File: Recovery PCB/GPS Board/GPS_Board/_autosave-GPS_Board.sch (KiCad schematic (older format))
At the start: 11 parts, among them J1 XT30-M, J2 XT30-M, U1 Teensy4.1

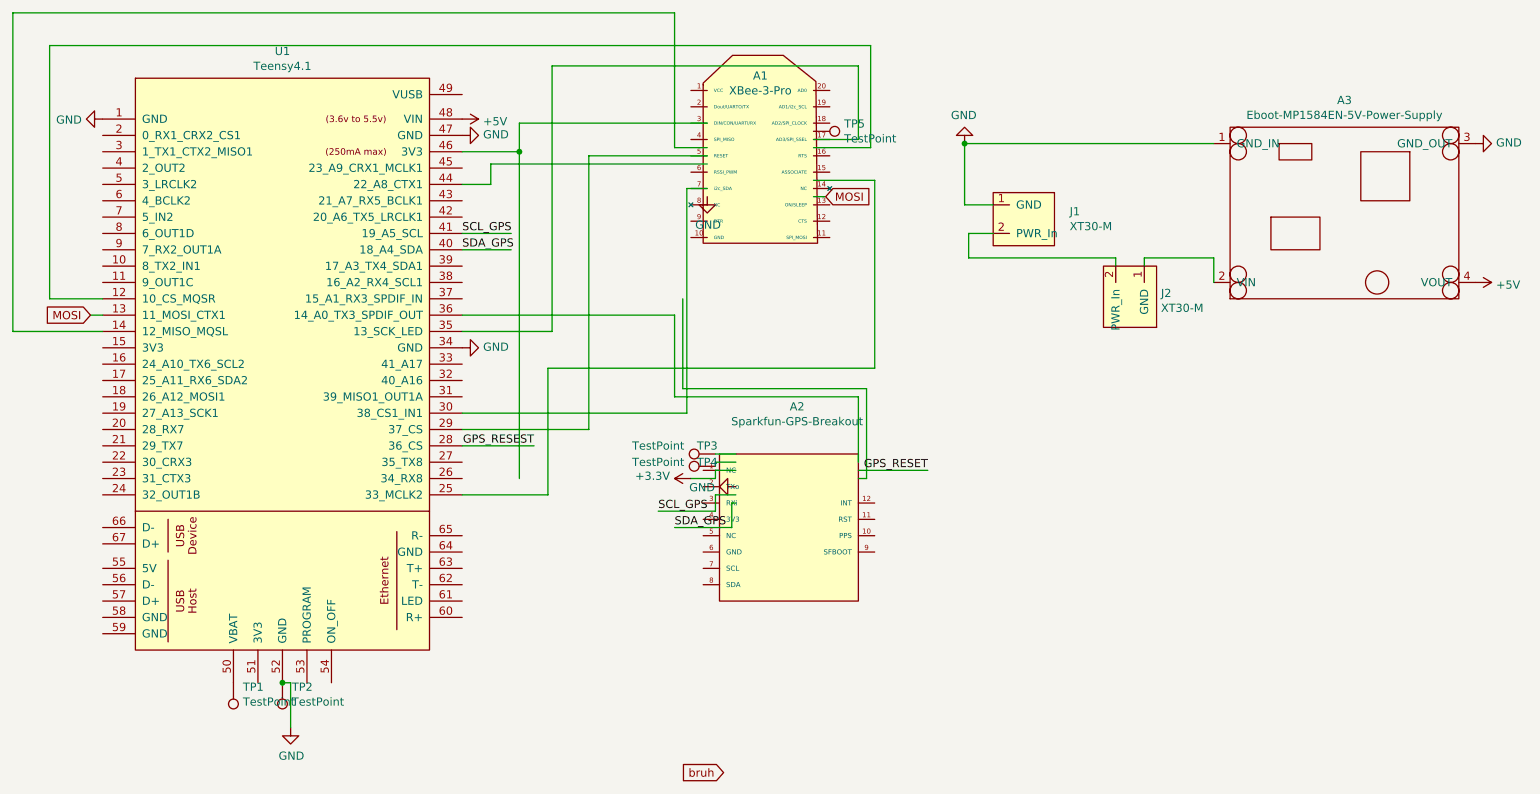
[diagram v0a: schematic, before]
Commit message: replace all wires w labels
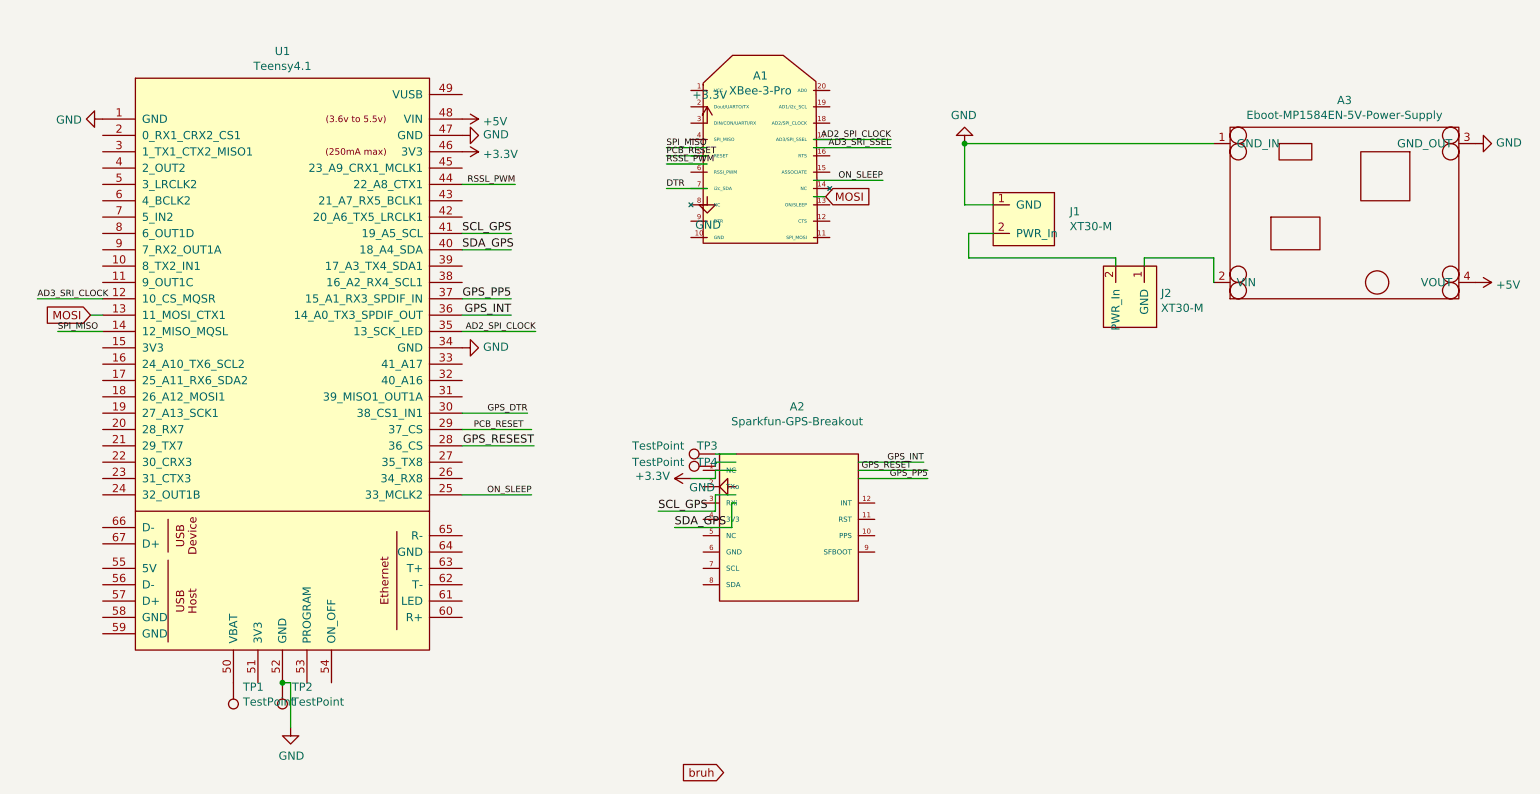
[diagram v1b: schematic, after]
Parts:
- removed TP5: TestPoint, TestPoint:TestPoint_Pad_D1.0mm, symbol Connector:TestPoint
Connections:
- net labels added: AD2_SPI_CLOCK, AD3_SRI_CLOCK, AD3_SRI_SSEL, DTR, GPS_DTR, GPS_INT, GPS_PP5, ON_SLEEP, PCB_RESET, RSSL_PWM, SPI_MISO
- wire segments 71 -> 48
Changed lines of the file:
@@
 	0    1    1    0
 $EndComp
-Wire Wire Line
-	4350 3600 4350 1600
-Wire Wire Line
-	4350 1600 4000 1600
 $Comp
 L power:GND #PWR0102
@@
 $EndComp
 Wire Wire Line
-	5300 3100 5300 2600
-Wire Wire Line
-	5300 2600 4000 2600
-Wire Wire Line
-	5350 2500 5350 3050
-Wire Wire Line
-	5350 3050 6475 3050
-Wire Wire Line
-	6475 3050 6475 3600
-Wire Wire Line
-	6475 3600 6425 3600
-Wire Wire Line
 	2900 4850 2950 4850
 Wire Wire Line
@@
 	1    0    0    -1
 $EndComp
-Wire Wire Line
-	5500 1425 4350 1425
-Wire Wire Line
-	4350 1425 4350 1600
-Connection ~ 4350 1600
-$Comp
-L Connector:TestPoint TP5
-U 1 1 61AB1BEF
-P 6150 1475
-F 0 "TP5" V 6104 1663 50  0000 L CNN
-F 1 "TestPoint" V 6195 1663 50  0000 L CNN
-F 2 "TestPoint:TestPoint_Pad_D1.0mm" H 6350 1475 50  0001 C CNN
-F 3 "~" H 6350 1475 50  0001 C CNN
-	1    6150 1475
-	0    1    1    0
-$EndComp
-Wire Wire Line
-	5500 1575 5300 1575
-Wire Wire Line
-	5300 1575 5300 750
-Wire Wire Line
-	5300 750  1250 750
-Wire Wire Line
-	1250 750  1250 2700
-Wire Wire Line
-	1250 2700 1800 2700
-Wire Wire Line
-	5500 1675 4175 1675
-Wire Wire Line
-	4175 1675 4175 1800
-Wire Wire Line
-	4175 1800 4000 1800
-Wire Wire Line
-	5500 1625 4775 1625
-Wire Wire Line
-	4775 1625 4775 3300
-Wire Wire Line
-	4775 3300 4000 3300
-Wire Wire Line
-	5500 1825 5375 1825
-Wire Wire Line
-	5375 1825 5375 3200
-Wire Wire Line
-	5375 3200 4000 3200
-Wire Wire Line
-	1800 2500 1475 2500
-Wire Wire Line
-	1475 2500 1475 950
-Wire Wire Line
-	1475 950  6500 950
-Wire Wire Line
-	6500 950  6500 1575
-Wire Wire Line
-	6500 1575 6150 1575
-Wire Wire Line
-	6150 1525 6425 1525
-Wire Wire Line
-	6425 1525 6425 1075
-Wire Wire Line
-	6425 1075 4550 1075
-Wire Wire Line
-	4550 1075 4550 2700
-Wire Wire Line
-	4550 2700 4000 2700
-Wire Wire Line
-	4525 2925 4525 3700
-Wire Wire Line
-	4525 3700 4000 3700
 Text GLabel 6225 1875 2    50   Input ~ 0
 MOSI
 Wire Wire Line
 	6150 1875 6225 1875
-Wire Wire Line
-	6150 1775 6525 1775
-Wire Wire Line
-	4525 2925 6525 2925
-Wire Wire Line
-	6525 1775 6525 2925
 Text GLabel 1725 2600 0    50   Input ~ 0
 MOSI
@@
 	0    -1   -1   0
 $EndComp
-Wire Wire Line
-	6425 3500 6425 3100
-Wire Wire Line
-	6425 3100 5300 3100
 Text GLabel 5600 5400 0    50   Input ~ 0
 bruh
@@
 Wire Wire Line
 	4000 3400 4440 3400
-Text Label 6850 3550 2    50   ~ 0
+Text Label 6750 3550 2    39   ~ 0
 GPS_RESET
 Wire Wire Line
 	6425 3550 6850 3550
+Wire Wire Line
+	6425 3600 6850 3600
+Text Label 4300 2500 2    50   ~ 0
+GPS_PP5
+Wire Wire Line
+	4000 2500 4300 2500
+Text Label 6850 3600 2    39   ~ 0
+GPS_PP5
+Wire Wire Line
+	6425 3500 6825 3500
+Wire Wire Line
+	4000 2600 4300 2600
+Text Label 4300 2600 2    50   ~ 0
+GPS_INT
+Text Label 6825 3500 2    39   ~ 0
+GPS_INT
+Text Label 4450 2700 2    39   ~ 0
+AD2_SPI_CLOCK
+Wire Wire Line
+	4000 2700 4450 2700
+Text Label 6625 1525 2    39   ~ 0
+AD2_SPI_CLOCK
+Wire Wire Line
+	6150 1525 6625 1525
+Wire Wire Line
+	6150 1575 6625 1575
+Text Label 6625 1575 2    39   ~ 0
+AD3_SRI_SSEL
+Text Label 1400 2500 0    39   ~ 0
+AD3_SRI_CLOCK
+Wire Wire Line
+	1400 2500 1800 2500
+$Comp
+L power:+3.3V #PWR?
+U 1 1 625CE6B8
+P 5500 1425
+F 0 "#PWR?" H 5500 1275 50  0001 C CNN
+F 1 "+3.3V" H 5515 1598 50  0000 C CNN
+F 2 "" H 5500 1425 50  0001 C CNN
+F 3 "" H 5500 1425 50  0001 C CNN
+	1    5500 1425
+	1    0    0    -1
+$EndComp
+Text Label 5250 1575 0    39   ~ 0
+SPI_MISO
+Wire Wire Line
+	5250 1575 5500 1575
+Text Label 1525 2700 0    39   ~ 0
+SPI_MISO
+Wire Wire Line
+	1800 2700 1525 2700
+Wire Wire Line
+	5500 1625 5250 1625
+Wire Wire Line
+	4000 3300 4425 3300
+Text Label 4375 3300 2    39   ~ 0
+PCB_RESET
+Text Label 5250 1625 0    39   ~ 0
+PCB_RESET
+Wire Wire Line
+	5500 1675 5250 1675
+Text Label 5250 1675 0    39   ~ 0
+RSSL_PWM
+Wire Wire Line
+	4000 1800 4325 1800
+Text Label 4325 1800 2    39   ~ 0
+RSSL_PWM
+Wire Wire Line
+	5500 1825 5250 1825
+Text Label 5250 1825 0    39   ~ 0
+DTR
+Wire Wire Line
+	4000 3200 4400 3200
+Text Label 4400 3200 2    39   ~ 0
+GPS_DTR
+Wire Wire Line
+	6150 1775 6575 1775
+Text Label 6575 1775 2    39   ~ 0
+ON_SLEEP
+Wire Wire Line
+	4000 3700 4425 3700
+Text Label 4425 3700 2    39   ~ 0
+ON_SLEEP
+$Comp
+L power:+3.3V #PWR?
+U 1 1 625E340B
+P 4000 1600
+F 0 "#PWR?" H 4000 1450 50  0001 C CNN
+F 1 "+3.3V" V 4015 1728 50  0000 L CNN
+F 2 "" H 4000 1600 50  0001 C CNN
+F 3 "" H 4000 1600 50  0001 C CNN
+	1    4000 1600
+	0    1    1    0
+$EndComp
 $EndSCHEMATC
